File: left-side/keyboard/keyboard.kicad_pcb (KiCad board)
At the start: 2 copper layers, 150.3 x 142 mm, 60 parts, among them SW1 SW_Push, SW10 SW_Push, SW11 SW_Push, SW12 SW_Push, SW13 SW_Push, SW14 SW_Push, SW15 SW_Push, SW16 SW_Push, SW17 SW_Push, SW18 SW_Push, SW19 SW_Push, SW2 SW_Push, SW20 SW_Push, SW21 SW_Push, SW22 SW_Push, SW23 SW_Push, SW24 SW_Push, SW25 SW_Push, SW26 SW_Push, SW27 SW_Push, SW3 SW_Push, SW4 SW_Push, SW5 SW_Push, SW6 SW_Push, SW7 SW_Push, SW8 SW_Push, SW9 SW_Push, U1 TRRS, U2 RP2040_Zero

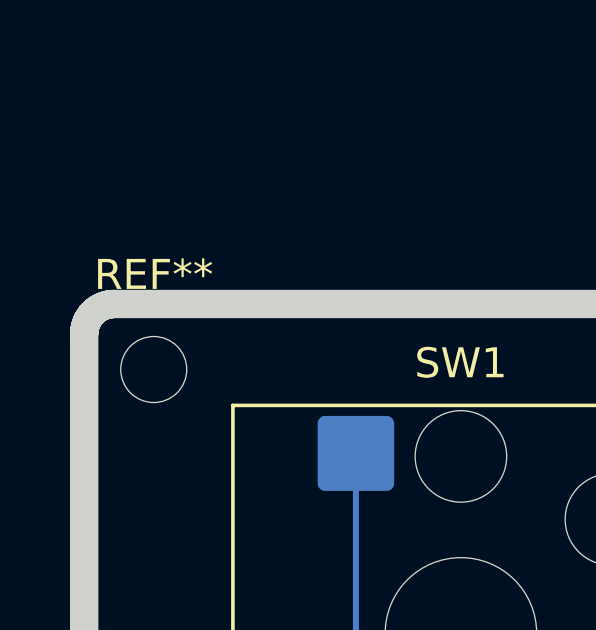
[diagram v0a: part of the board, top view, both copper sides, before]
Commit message: Match screw on left side
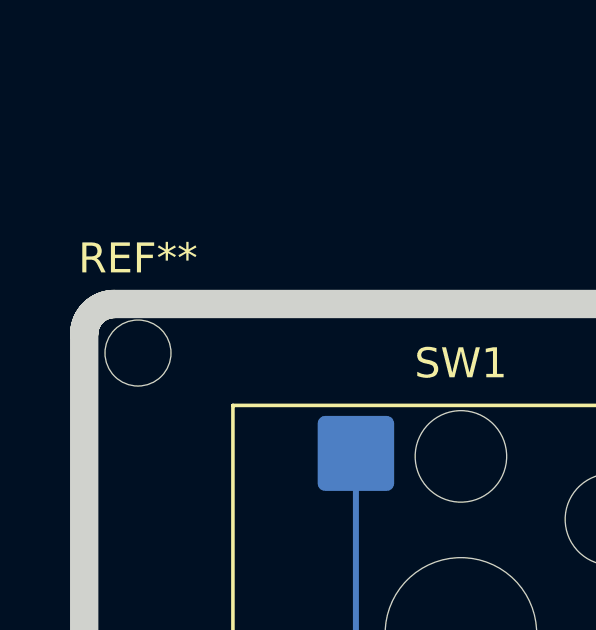
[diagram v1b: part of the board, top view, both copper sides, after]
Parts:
- moved REF** 0.76 mm to (33.2, 29.7)
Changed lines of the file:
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@@
 	(footprint "MountingHole:MountingHole_2.2mm_M2"
 		(layer "F.Cu")
-		(at 33.75 30.25)
+		(at 33.225 29.7)
 		(descr "Mounting Hole 2.2mm, M2, no annular, generated by kicad-footprint-generator mountinghole.py")
 		(tags "mountinghole M2")
